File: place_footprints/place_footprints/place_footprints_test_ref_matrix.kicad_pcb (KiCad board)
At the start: 2 copper layers, 64 parts

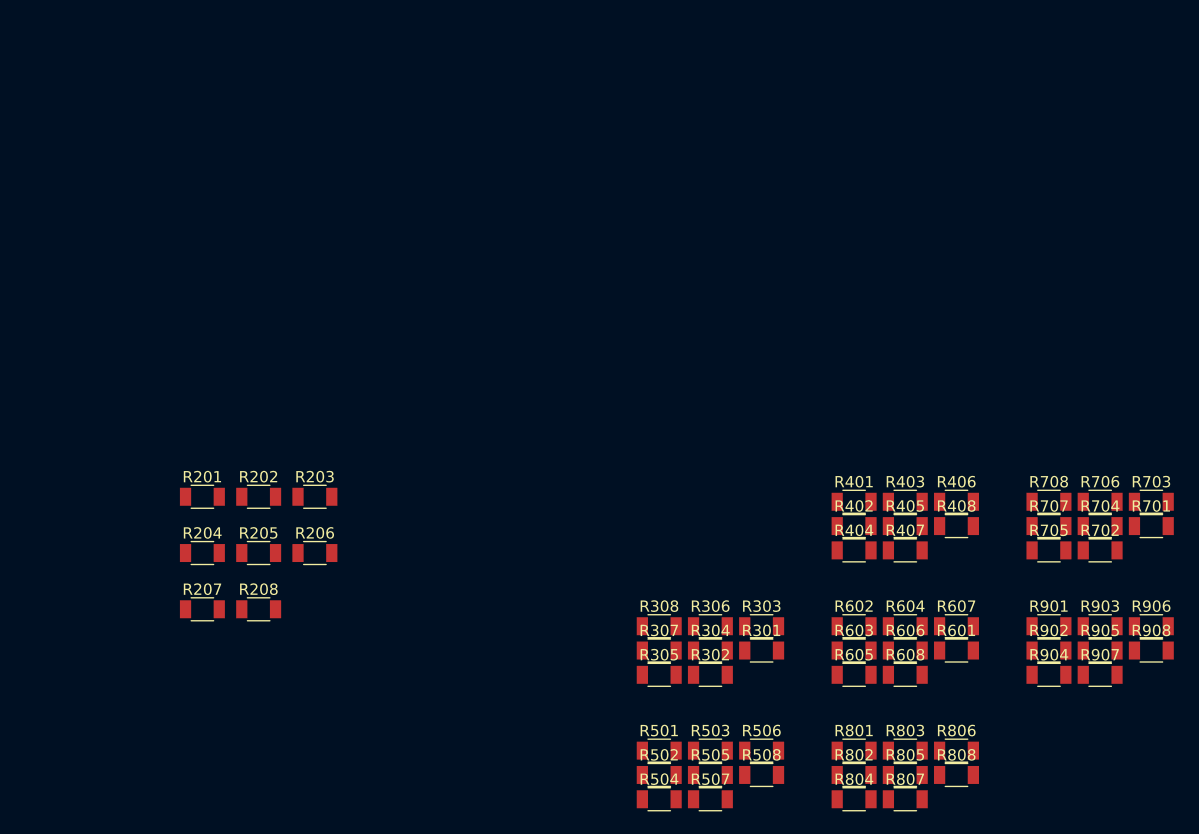
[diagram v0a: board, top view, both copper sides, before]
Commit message: Fixed circular placement
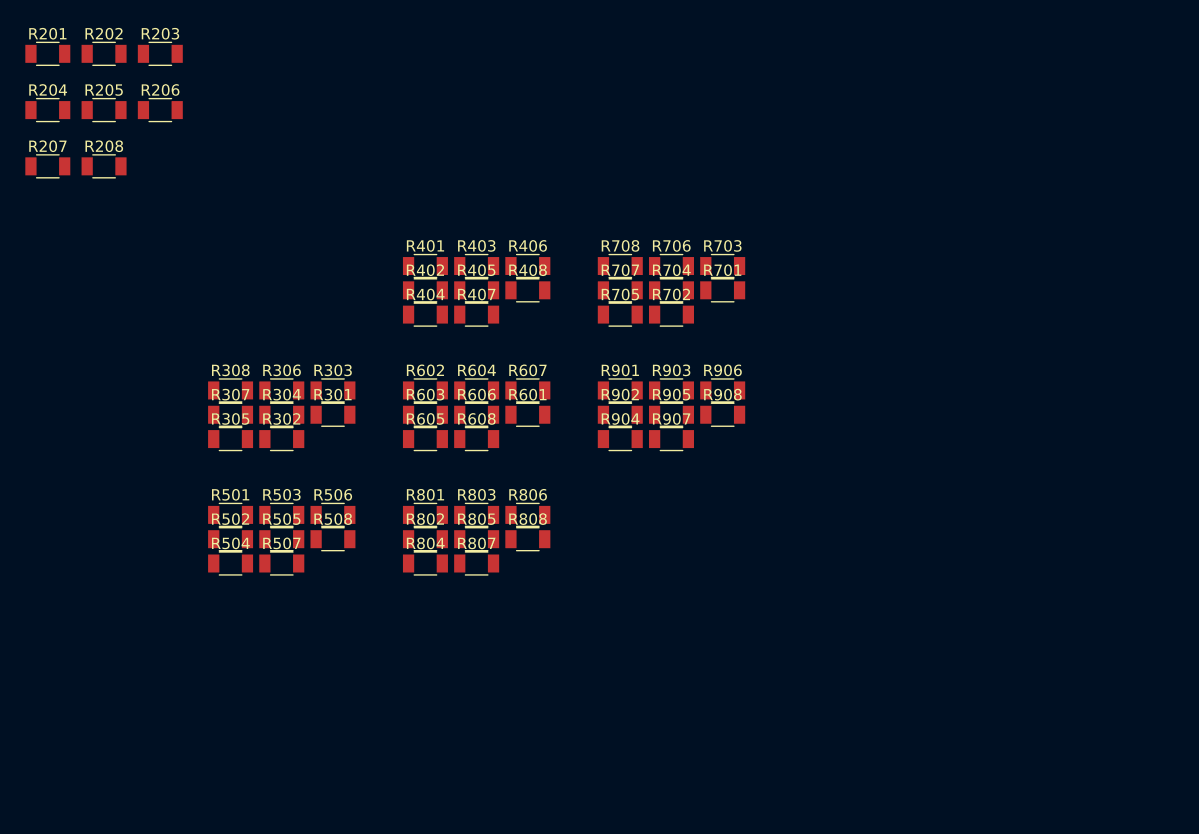
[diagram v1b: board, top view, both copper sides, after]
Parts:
- moved R301 43.5 mm to (69.2, 61.3)
- moved R302 43.5 mm to (64.6, 63.5)
- moved R303 43.5 mm to (69.2, 59.1)
- moved R304 43.5 mm to (64.6, 61.3)
- moved R306 43.5 mm to (64.6, 59.1)
- moved R401 43.5 mm to (77.4, 48.1)
- moved R402 43.5 mm to (77.4, 50.2)
- moved R404 43.5 mm to (77.4, 52.4)
- moved R503 43.5 mm to (64.6, 70.2)
- moved R505 43.5 mm to (64.6, 72.4)
- moved R506 43.5 mm to (69.2, 70.2)
- moved R507 43.5 mm to (64.6, 74.5)
- moved R508 43.5 mm to (69.2, 72.4)
- moved R602 43.5 mm to (77.4, 59.1)
- moved R603 43.5 mm to (77.4, 61.3)
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
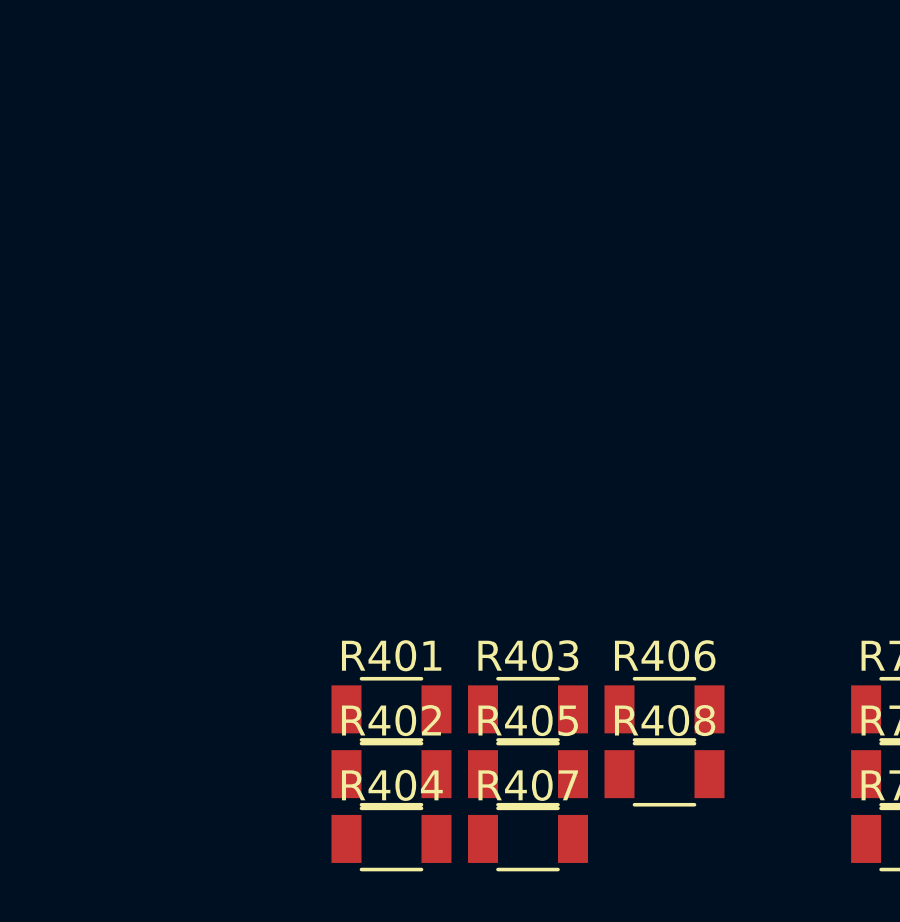
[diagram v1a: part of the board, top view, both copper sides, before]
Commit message: added support for any footprint to serve as a reference in linear and circular mode
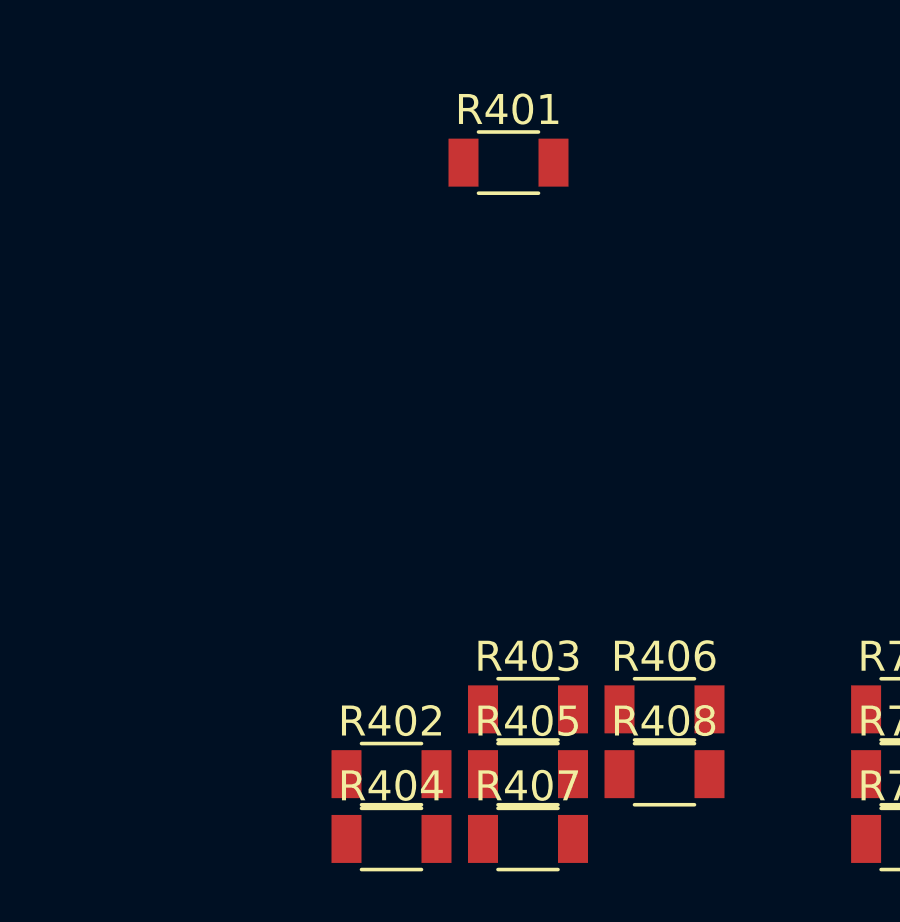
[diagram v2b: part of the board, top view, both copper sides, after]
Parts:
- moved R401 18.6 mm to (81.3, 29.8)
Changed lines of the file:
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@@
-(kicad_pcb (version 20171130) (host pcbnew "(5.0.2)-1")
+(kicad_pcb (version 20171130) (host pcbnew "(5.1.0-rc2-4-g73f0b3087)")
   (general
     (thickness 1.6)
@@
     (zone_45_only no)
     (trace_min 0.2)
-    (segment_width 0.2)
-    (edge_width 0.15)
     (via_size 0.8)
     (via_drill 0.4)
@@
     (uvia_min_size 0.2)
     (uvia_min_drill 0.1)
+    (edge_width 0.15)
+    (segment_width 0.2)
     (pcb_text_width 0.3)
     (pcb_text_size 1.5 1.5)
@@
   )
   (module Passives:R1206M (layer F.Cu)
-    (at 77.380001 48.070001)
-    (descr "Capacitor SMD 1206, reflow soldering, AVX (see smccp.pdf)")
-    (tags "capacitor 1206")
+    (at 81.28 29.845)
+    (descr "Capacitor SMD 1206, reflow soldering, AVX (see smccp.pdf)")
+    (tags "capacitor 1206")

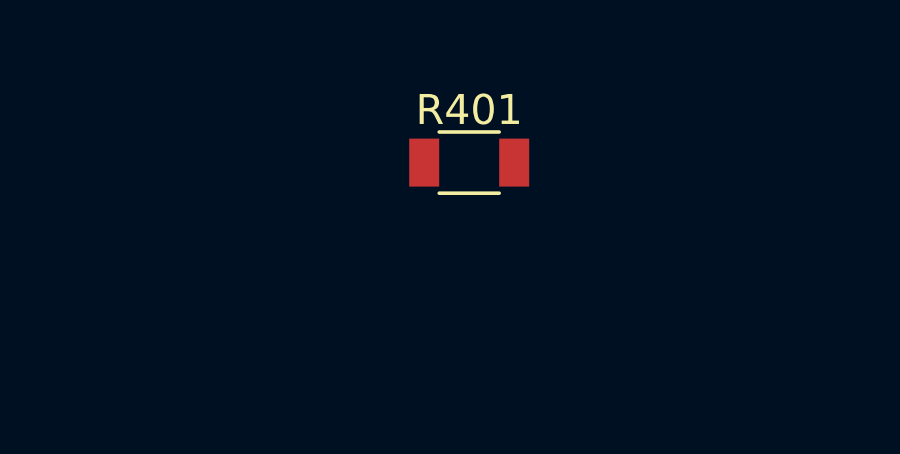
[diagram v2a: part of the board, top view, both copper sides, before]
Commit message: updated test cases
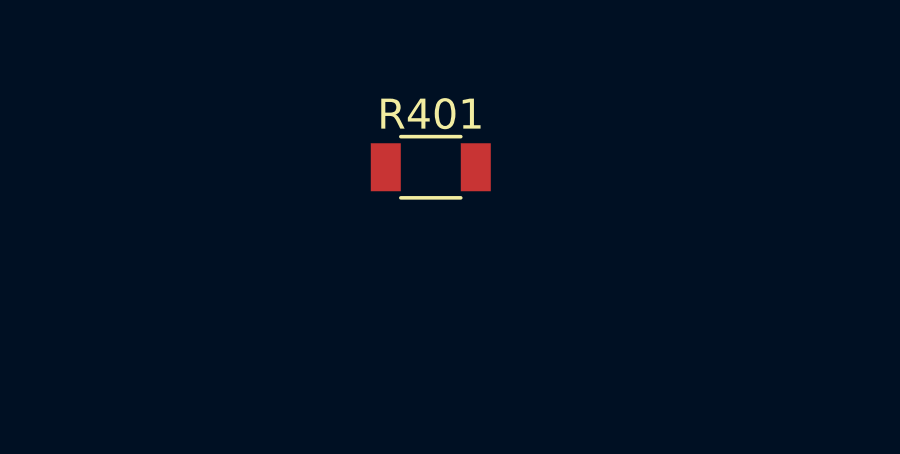
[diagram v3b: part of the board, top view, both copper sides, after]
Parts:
- moved R401 1.29 mm to (80.0, 30.0)
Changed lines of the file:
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@@
-(kicad_pcb (version 20171130) (host pcbnew "(5.1.0-rc2-4-g73f0b3087)")
+(kicad_pcb (version 20171130) (host pcbnew "(5.1.5-90-g5c7ac1bb7)-1")
   (general
     (thickness 1.6)
@@
   )
   (module Passives:R1206M (layer F.Cu)
-    (at 81.28 29.845)
-    (descr "Capacitor SMD 1206, reflow soldering, AVX (see smccp.pdf)")
-    (tags "capacitor 1206")
+    (at 80 30)
+    (descr "Capacitor SMD 1206, reflow soldering, AVX (see smccp.pdf)")
+    (tags "capacitor 1206")
